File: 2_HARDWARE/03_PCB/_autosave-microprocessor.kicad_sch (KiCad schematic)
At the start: 29 parts, among them SW1 TS-1187A-B-A-B, U11 STM32F446ZETx, Y1 32.768k

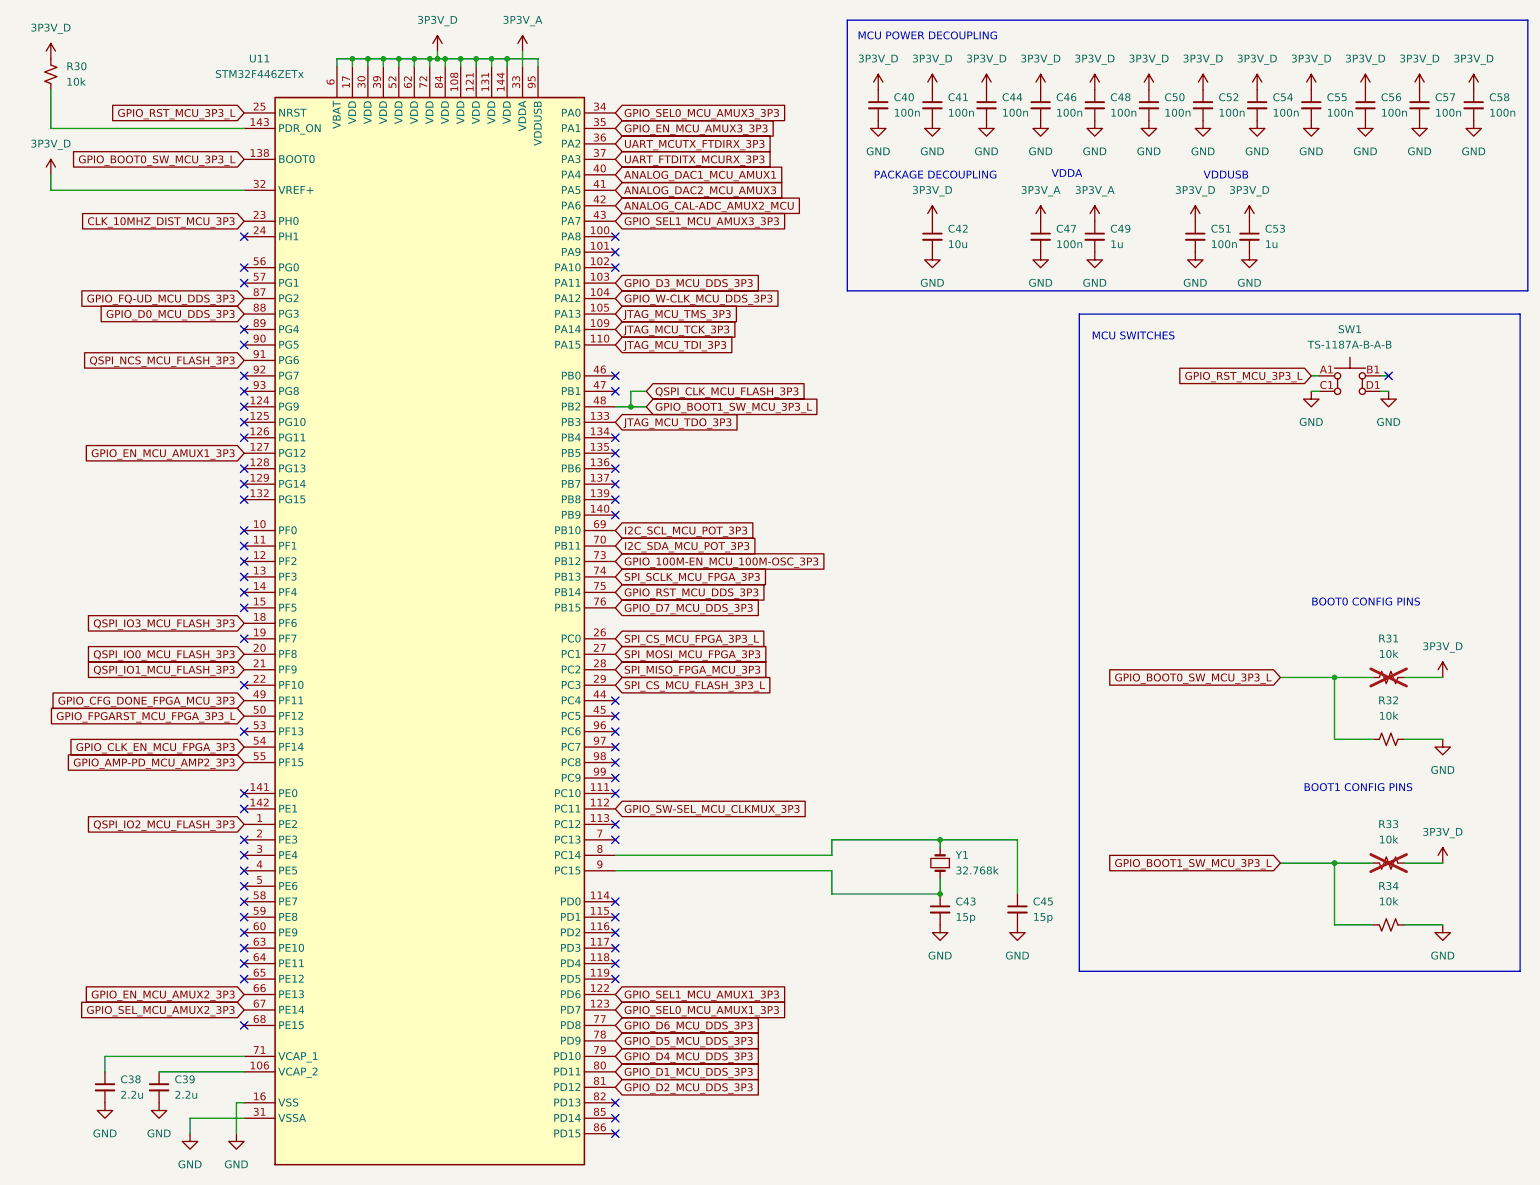
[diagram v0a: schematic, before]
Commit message: FEAT: Routed Analog and all Misc Signals. Routing is complete.
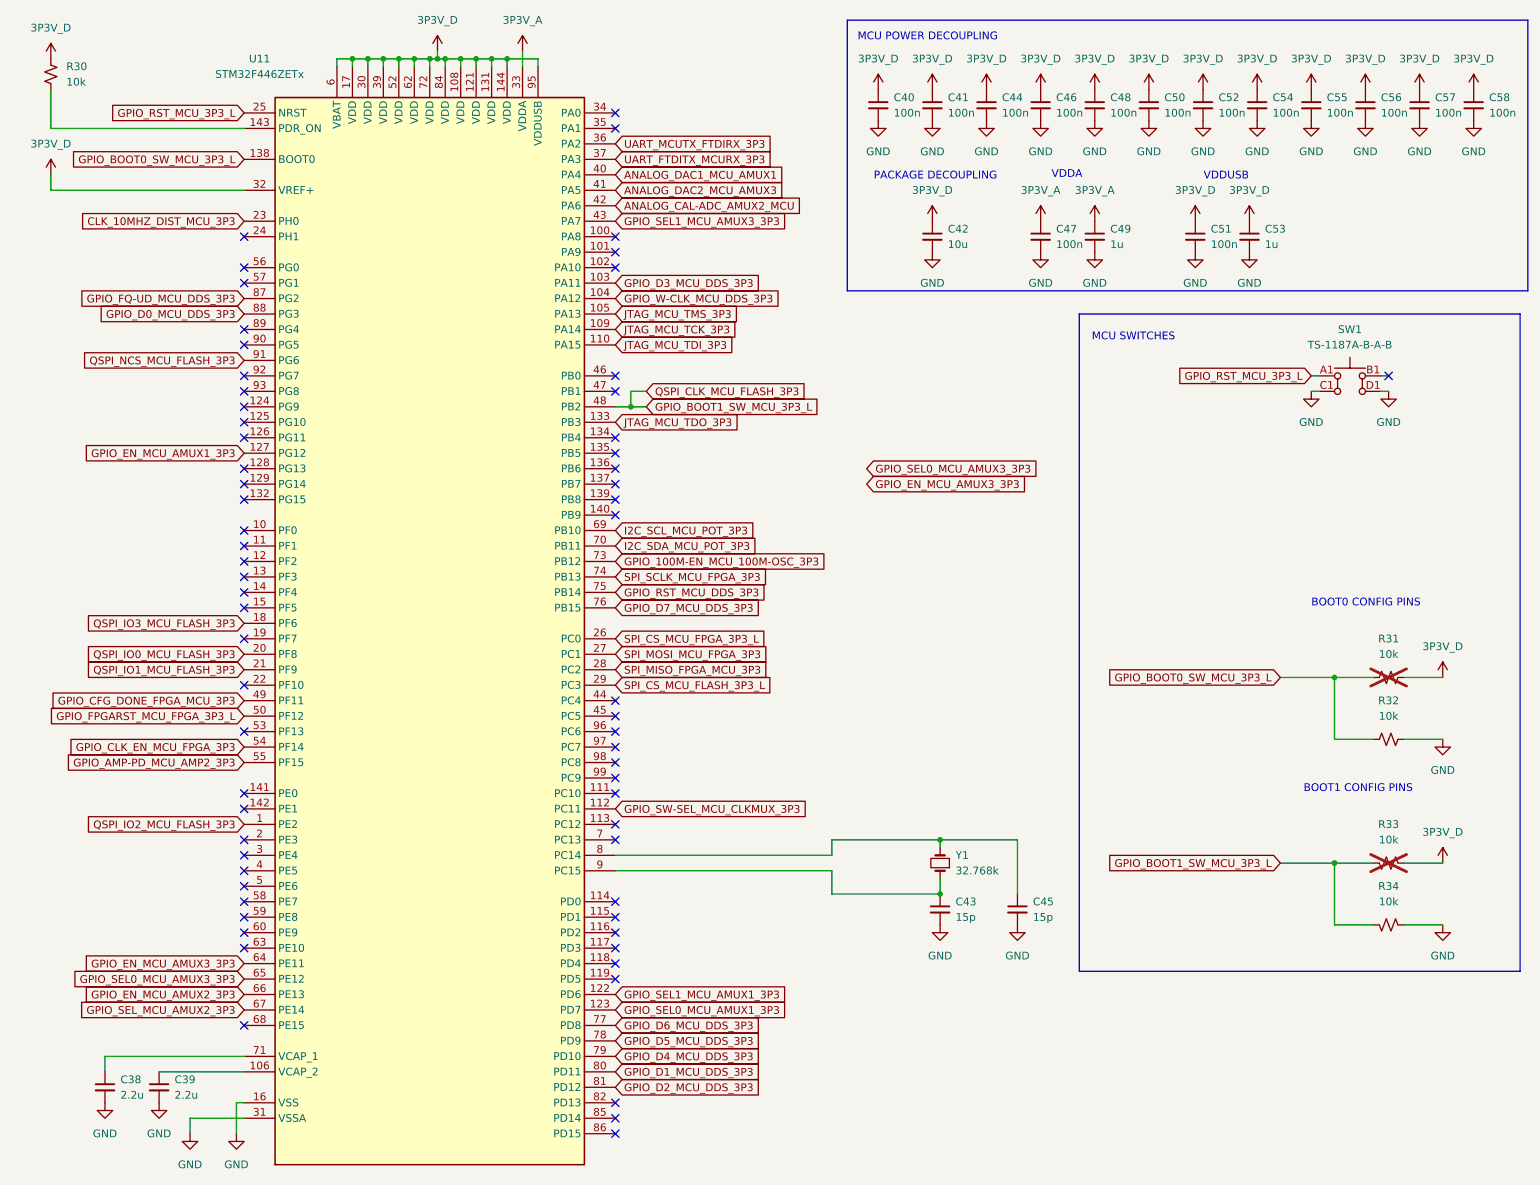
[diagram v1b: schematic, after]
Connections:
- net GPIO_EN_MCU_AMUX3_3P3: now also U11.64 (PE11); no longer U11.35 (PA1)
- net GPIO_SEL0_MCU_AMUX3_3P3: now also U11.65 (PE12); no longer U11.34 (PA0)
